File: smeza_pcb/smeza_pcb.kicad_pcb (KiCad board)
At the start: 2 copper layers, 76.2 x 76.2 mm, 59 parts, among them J1 SS-90000-002, J2 SS-90000-002, J3 Conn_01x03, J4 Conn_01x04, J5 Conn_01x03, J6 Conn_01x03, J7 Conn_01x03, J8 Conn_01x03, J9 Conn_02x03_Odd_Even, SW1 SW_DIP_x04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

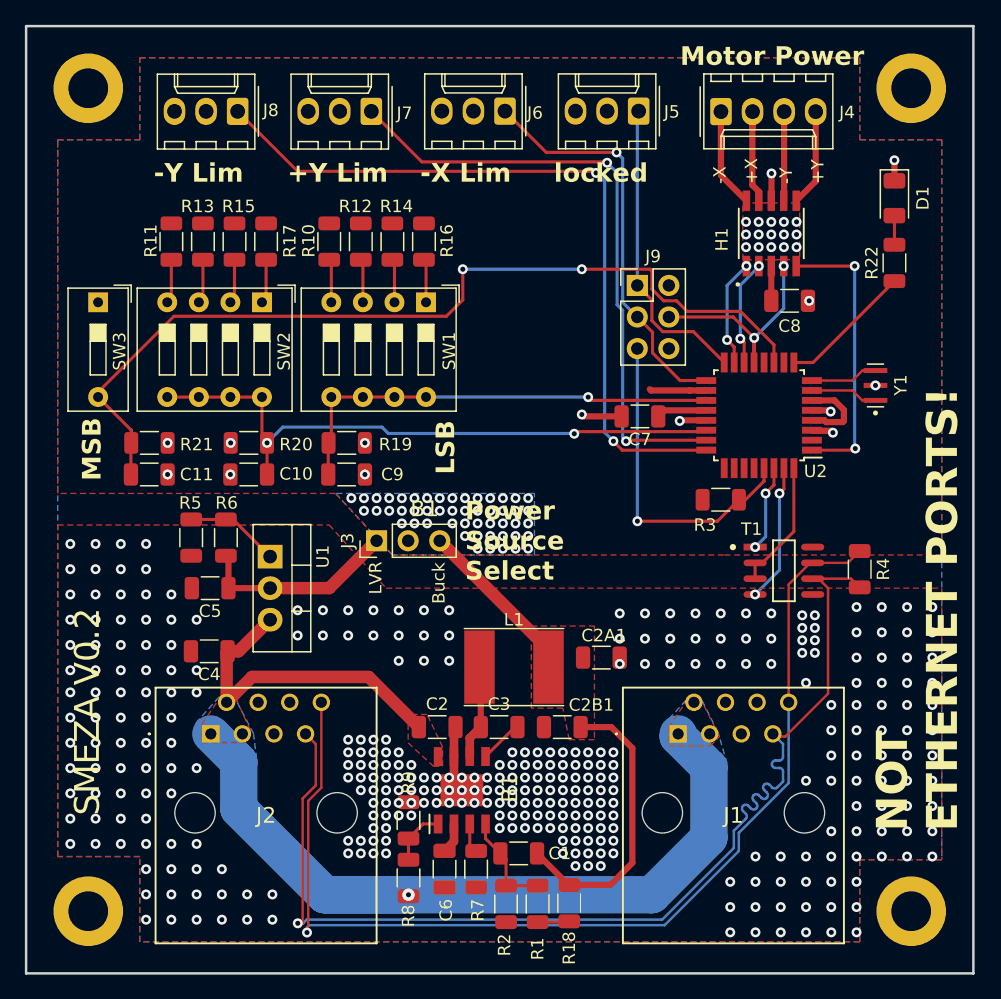
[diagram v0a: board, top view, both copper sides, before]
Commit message: Moved vias out from under pads
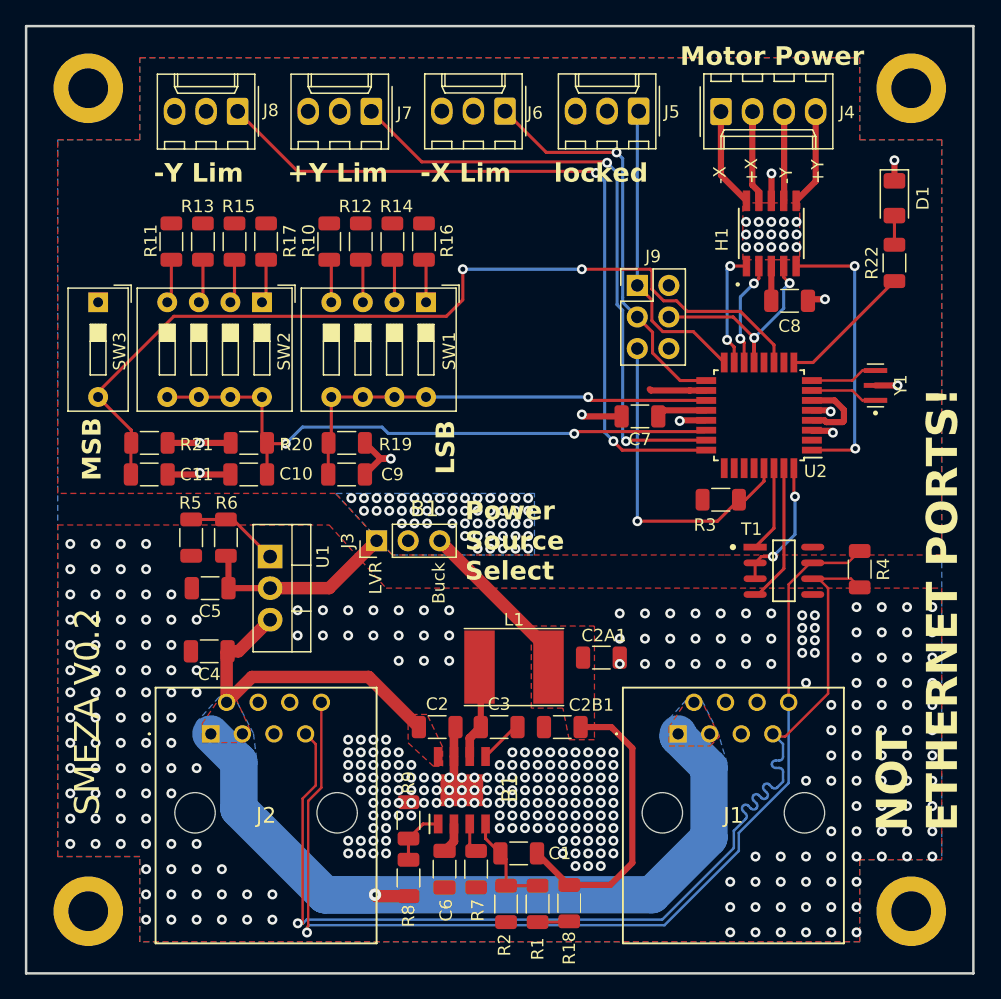
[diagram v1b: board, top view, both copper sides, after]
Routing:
- net GND: track 19.6 -> 38.2 mm, vias 375 -> 372
- net /TransceiverDriverEnable: track 10.5 -> 11.4 mm, vias 0 -> 2
- net /M1 Bkwd Signal: track 8.64 -> 9.40 mm
- net /Tx: track 11.1 -> 11.3 mm, vias 2 -> 0
- net /Rx: vias 2 -> 0

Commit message: Updated version text on board
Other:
- board text added: "SMEZA V0.3"
- board text removed: "SMEZA V0.2"
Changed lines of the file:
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@@
     (effects (font (size 1.5 1.5) (thickness 0.3) bold) (justify left bottom))
   )
-  (gr_text "SMEZA V0.2" (at 107.696 116.84 90) (layer "F.SilkS")
+  (gr_text "SMEZA V0.3" (at 107.696 116.84 90) (layer "F.SilkS")
     (effects (font (size 2 2) (thickness 0.3)) (justify left bottom))
   )

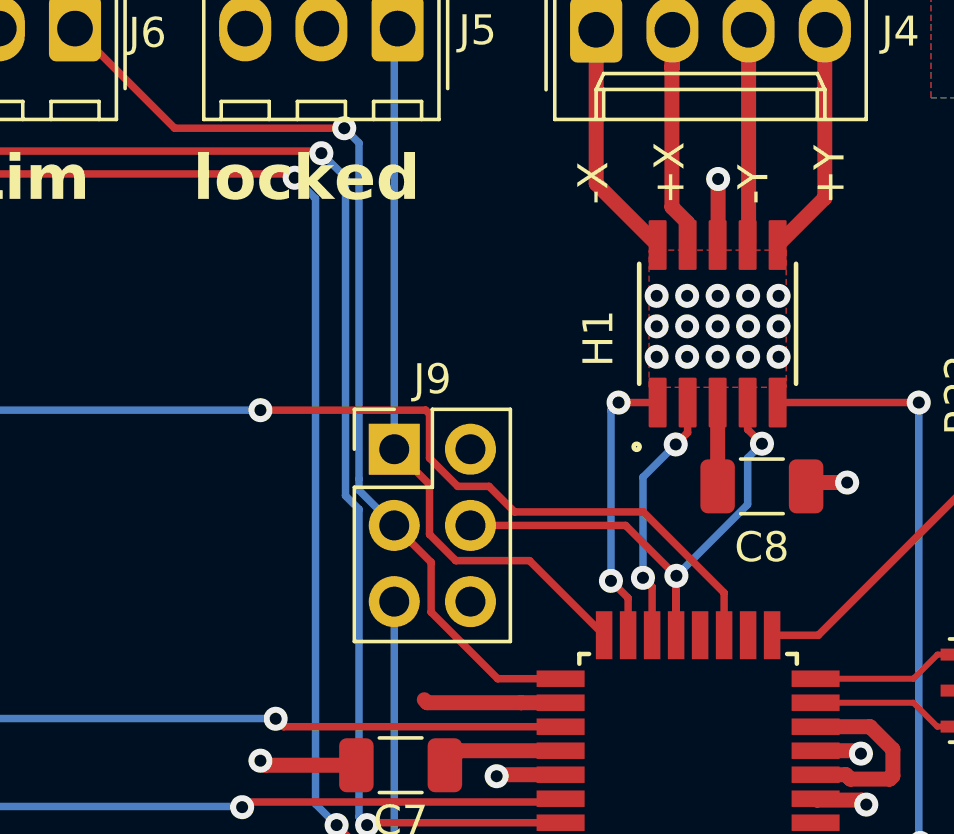
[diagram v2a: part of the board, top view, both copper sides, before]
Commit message: Separated MOSI and M2 Bkwd pins
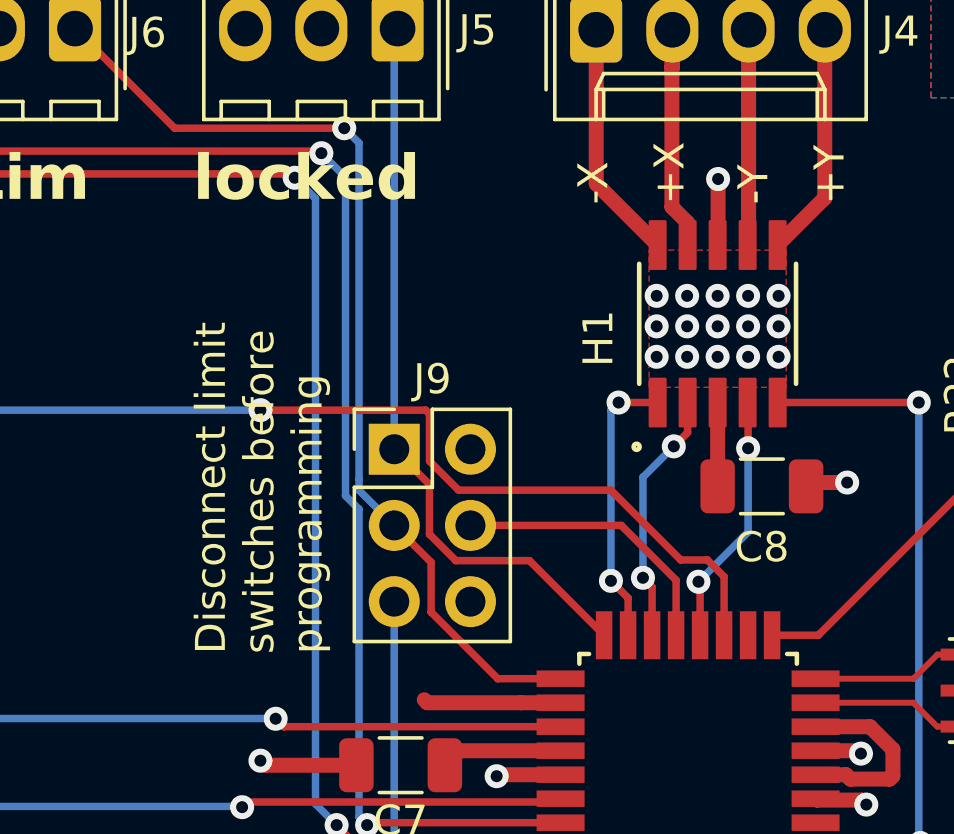
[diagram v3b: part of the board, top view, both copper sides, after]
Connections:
- H1 pad 4: /M2 Bkwd Signal (MOSI) -> /M2 Bkwd Signal
- J9 pad 4: /M2 Bkwd Signal (MOSI) -> /MOSI
- U2 pad 12: unconnected-(U2-PB0-Pad12) -> /M2 Bkwd Signal
- U2 pad 13: /M2 Bkwd Signal (MOSI) -> /MOSI
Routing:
- net /M2 Bkwd Signal (MOSI): track 18.7 -> 0.00 mm, vias 2 -> 0
- net /MOSI: track 0.00 -> 9.45 mm
- net /M2 Bkwd Signal: track 0.00 -> 8.47 mm, vias 0 -> 2
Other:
- board text added: "Disconnect limit switches before programming"
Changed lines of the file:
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@@
   (net 35 "Net-(U2-AREF)")
   (net 36 "/M2 Fwd Signal")
-  (net 37 "/M2 Bkwd Signal (MOSI)")
+  (net 37 "/M2 Bkwd Signal")
   (net 38 "/M1 Fwd Signal")
   (net 39 "/M1 Bkwd Signal")
@@
   (net 47 "Net-(U2-XTAL2{slash}PB7)")
   (net 48 "unconnected-(U2-PD6-Pad10)")
-  (net 49 "unconnected-(U2-PB0-Pad12)")
+  (net 49 "/MOSI")
   (net 50 "unconnected-(U2-PC2-Pad25)")
   (net 51 "unconnected-(U2-PC3-Pad26)")
@@
       (net 41 "/M1 -Limit (SCK)") (pinfunction "Pin_3") (pintype "passive"))
     (pad "4" thru_hole oval (at 2.54 2.54) (size 1.7 1.7) (drill 1) (layers "*.Cu" "*.Mask")
-      (net 37 "/M2 Bkwd Signal (MOSI)") (pinfunction "Pin_4") (pintype "passive"))
+      (net 49 "/MOSI") (pinfunction "Pin_4") (pintype "passive"))
     (pad "5" thru_hole oval (at 0 5.08) (size 1.7 1.7) (drill 1) (layers "*.Cu" "*.Mask")
       (net 44 "/RESET") (pinfunction "Pin_5") (pintype "passive"))
@@
       (net 34 "/DIP9") (pinfunction "PD7") (pintype "bidirectional"))
     (pad "12" smd rect (at -0.4 4.25 270) (size 1.6 0.55) (layers "F.Cu" "F.Paste" "F.Mask")
-      (net 49 "unconnected-(U2-PB0-Pad12)") (pinfunction "PB0") (pintype "bidirectional+no_connect"))
+      (net 37 "/M2 Bkwd Signal") (pinfunction "PB0") (pintype "bidirectional"))
     (pad "13" smd rect (at 0.4 4.25 270) (size 1.6 0.55) (layers "F.Cu" "F.Paste" "F.Mask")
-      (net 37 "/M2 Bkwd Signal (MOSI)") (pinfunction "PB1") (pintype "bidirectional"))
+      (net 49 "/MOSI") (pinfunction "PB1") (pintype "bidirectional"))
     (pad "14" smd rect (at 1.2 4.25 270) (size 1.6 0.55) (layers "F.Cu" "F.Paste" "F.Mask")
       (net 38 "/M1 Fwd Signal") (pinfunction "PB2") (pintype "bidirectional"))
@@
       (net 10 "/+5V") (pinfunction "VBB") (pintype "passive") (zone_connect 2))
     (pad "4" smd roundrect (at -2.625 1 90) (size 1.66 0.6) (layers "F.Cu" "F.Paste" "F.Mask") (roundrect_rratio 0.07)
-      (net 37 "/M2 Bkwd Signal (MOSI)") (pinfunction "IN3") (pintype "passive"))
+      (net 37 "/M2 Bkwd Signal") (pinfunction "IN3") (pintype "passive"))
     (pad "5" smd roundrect (at -2.625 2 90) (size 1.66 0.6) (layers "F.Cu" "F.Paste" "F.Mask") (roundrect_rratio 0.07)
       (net 36 "/M2 Fwd Signal") (pinfunction "IN4") (pintype "passive"))
@@
     (effects (font (size 1.5 1.5) (thickness 0.3) bold) (justify left bottom))
   )
+  (gr_text "Disconnect limit \nswitches before \nprogramming" (at 148.463 81.026 90) (layer "F.SilkS")
+    (effects (font (size 1 1) (thickness 0.153)) (justify left bottom))
+  )
   (gr_text "+Y\n" (at 165.862 66.04 90) (layer "F.SilkS")
     (effects (font (size 1 1) (thickness 0.153)) (justify left bottom))
@@
   (segment (start 130.7338 86.106) (end 145.669 86.106) (width 0.25) (layer "B.Cu") (net 33))
   (segment (start 123.825 85.598) (end 130.2258 85.598) (width 0.25) (layer "B.Cu") (net 33))
-  (segment (start 151.94 73.025) (end 151.813 72.898) (width 0.25) (layer "F.Cu") (net 34))
+  (segment (start 160.315299 77.892299) (end 157.988 75.565) (width 0.25) (layer "F.Cu") (net 34))
+  (segment (start 157.988 75.565) (end 152.908 75.565) (width 0.25) (layer "F.Cu") (net 34))
   (segment (start 110.0582 86.868) (end 110.0582 85.8437) (width 0.25) (layer "F.Cu") (net 34))
+  (segment (start 161.205006 77.892299) (end 160.315299 77.892299) (width 0.25) (layer "F.Cu") (net 34))
   (segment (start 107.3912 82.7786) (end 107.3912 83.1767) (width 0.25) (layer "F.Cu") (net 34))
-  (segment (start 161.76 80.4) (end 161.76 78.984973) (width 0.25) (layer "F.Cu") (net 34))
+  (segment (start 161.76 78.447293) (end 161.205006 77.892299) (width 0.25) (layer "F.Cu") (net 34))
   (segment (start 110.031 89.408) (end 110.031 86.8952) (width 0.25) (layer "F.Cu") (net 34))
-  (segment (start 159.065027 76.29) (end 154.776 76.29) (width 0.25) (layer "F.Cu") (net 34))
-  (segment (start 151.813 72.898) (end 146.304 72.898) (width 0.25) (layer "F.Cu") (net 34))
+  (segment (start 151.94 73.025) (end 151.813 72.898) (width 0.25) (layer "F.Cu") (net 34))
   (segment (start 110.0582 85.8437) (end 107.3912 83.1767) (width 0.25) (layer "F.Cu") (net 34))
   (segment (start 110.031 86.8952) (end 110.0582 86.868) (width 0.25) (layer "F.Cu") (net 34))
+  (segment (start 152.908 75.565) (end 151.94 74.597) (width 0.25) (layer "F.Cu") (net 34))
   (segment (start 113.4881 76.6817) (end 107.3912 82.7786) (width 0.25) (layer "F.Cu") (net 34))
-  (segment (start 152.881299 75.438) (end 151.94 74.496701) (width 0.25) (layer "F.Cu") (net 34))
   (segment (start 136.7282 72.898) (end 136.7282 75.3618) (width 0.25) (layer "F.Cu") (net 34))
+  (segment (start 151.813 72.898) (end 146.304 72.898) (width 0.25) (layer "F.Cu") (net 34))
   (segment (start 135.4083 76.6817) (end 113.4881 76.6817) (width 0.25) (layer "F.Cu") (net 34))
-  (segment (start 154.776 76.29) (end 153.924 75.438) (width 0.25) (layer "F.Cu") (net 34))
   (segment (start 136.7282 75.3618) (end 135.4083 76.6817) (width 0.25) (layer "F.Cu") (net 34))
-  (segment (start 151.94 74.496701) (end 151.94 73.025) (width 0.25) (layer "F.Cu") (net 34))
-  (segment (start 153.924 75.438) (end 152.881299 75.438) (width 0.25) (layer "F.Cu") (net 34))
-  (segment (start 161.76 78.984973) (end 159.065027 76.29) (width 0.25) (layer "F.Cu") (net 34))
+  (segment (start 151.94 74.597) (end 151.94 73.025) (width 0.25) (layer "F.Cu") (net 34))
+  (segment (start 161.76 80.4) (end 161.76 78.447293) (width 0.25) (layer "F.Cu") (net 34))
   (via (at 146.304 72.898) (size 0.8) (drill 0.4) (layers "F.Cu" "B.Cu") (net 34))
   (via (at 136.7282 72.898) (size 0.8) (drill 0.4) (layers "F.Cu" "B.Cu") (net 34))
@@
   (segment (start 168.3004 87.3252) (end 168.2496 87.2744) (width 0.25) (layer "B.Cu") (net 36))
   (segment (start 168.2496 87.2744) (end 168.2496 72.644) (width 0.25) (layer "B.Cu") (net 36))
-  (segment (start 162.544 73.538856) (end 162.544 72.644) (width 0.25) (layer "F.Cu") (net 37))
-  (segment (start 160.16 80.4) (end 160.16 78.42985) (width 0.25) (layer "F.Cu") (net 37))
-  (segment (start 158.4772 76.74) (end 153.305 76.74) (width 0.25) (layer "F.Cu") (net 37))
-  (segment (start 160.16 78.4228) (end 158.4772 76.74) (width 0.25) (layer "F.Cu") (net 37))
-  (segment (start 160.16 78.42985) (end 160.169786 78.420064) (width 0.25) (layer "F.Cu") (net 37))
-  (segment (start 160.16 80.4) (end 160.16 78.4228) (width 0.25) (layer "F.Cu") (net 37))
-  (segment (start 163.021642 74.016498) (end 162.544 73.538856) (width 0.25) (layer "F.Cu") (net 37))
-  (via (at 160.169786 78.420064) (size 0.8) (drill 0.4) (layers "F.Cu" "B.Cu") (net 37))
-  (via (at 163.021642 74.016498) (size 0.8) (drill 0.4) (layers "F.Cu" "B.Cu") (net 37))
-  (segment (start 162.543998 74.494142) (end 162.543998 76.045852) (width 0.25) (layer "B.Cu") (net 37))
-  (segment (start 162.543998 76.045852) (end 160.169786 78.420064) (width 0.25) (layer "B.Cu") (net 37))
-  (segment (start 163.021642 74.016498) (end 162.543998 74.494142) (width 0.25) (layer "B.Cu") (net 37))
-  (segment (start 160.147 74.041) (end 160.544 73.644) (width 0.25) (layer "F.Cu") (net 38))
+  (segment (start 162.56 72.66) (end 162.544 72.644) (width 0.25) (layer "F.Cu") (net 37))
+  (segment (start 162.56 74.168) (end 162.56 72.66) (width 0.25) (layer "F.Cu") (net 37))
+  (segment (start 160.96 78.672598) (end 160.904701 78.617299) (width 0.25) (layer "F.Cu") (net 37))
+  (segment (start 160.96 80.4) (end 160.96 78.672598) (width 0.25) (layer "F.Cu") (net 37))
+  (via (at 162.56 74.168) (size 0.8) (drill 0.4) (layers "F.Cu" "B.Cu") (net 37))
+  (via (at 160.904701 78.617299) (size 0.8) (drill 0.4) (layers "F.Cu" "B.Cu") (net 37))
+  (segment (start 160.904701 78.617299) (end 162.56 76.962) (width 0.25) (layer "B.Cu") (net 37))
+  (segment (start 162.56 76.962) (end 162.56 74.168) (width 0.25) (layer "B.Cu") (net 37))
   (segment (start 160.544 73.644) (end 160.544 72.644) (width 0.25) (layer "F.Cu") (net 38))
+  (segment (start 160.0835 74.1045) (end 160.544 73.644) (width 0.25) (layer "F.Cu") (net 38))
   (segment (start 159.36 80.4) (end 159.36 78.7912) (width 0.25) (layer "F.Cu") (net 38))
   (segment (start 159.36 78.7912) (end 159.0548 78.486) (width 0.25) (layer "F.Cu") (net 38))
-  (via (at 160.147 74.041) (size 0.8) (drill 0.4) (layers "F.Cu" "B.Cu") (net 38))
+  (via (at 160.0835 74.1045) (size 0.8) (drill 0.4) (layers "F.Cu" "B.Cu") (net 38))
   (via (at 159.0548 78.486) (size 0.8) (drill 0.4) (layers "F.Cu" "B.Cu") (net 38))
-  (segment (start 160.147 74.041) (end 159.0548 75.1332) (width 0.25) (layer "B.Cu") (net 38))
+  (segment (start 160.0835 74.1045) (end 159.0548 75.1332) (width 0.25) (layer "B.Cu") (net 38))
   (segment (start 159.0548 75.1332) (end 159.0548 78.486) (width 0.25) (layer "B.Cu") (net 38))
   (segment (start 158.56 80.4) (end 158.56 79.1596) (width 0.25) (layer "F.Cu") (net 39))
@@
   (segment (start 168.8738 81.0452) (end 169.926 81.0452) (width 0.2) (layer "F.Cu") (net 47))
   (segment (start 164.81 81.85) (end 168.069 81.85) (width 0.2) (layer "F.Cu") (net 47))
+  (segment (start 158.334105 76.74) (end 153.305 76.74) (width 0.25) (layer "F.Cu") (net 49))
+  (segment (start 160.16 80.4) (end 160.16 78.565895) (width 0.25) (layer "F.Cu") (net 49))
+  (segment (start 160.16 78.565895) (end 158.334105 76.74) (width 0.25) (layer "F.Cu") (net 49))
   (segment (start 135.259 119.683) (end 136.017 118.925) (width 0.7) (layer "F.Cu") (net 54))
   (segment (start 136.017 118.925) (end 136.017 117.52) (width 0.7) (layer "F.Cu") (net 54))
